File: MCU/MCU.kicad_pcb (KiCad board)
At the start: 4 copper layers, 55 x 62 mm, 52 parts, among them IC1 STM32G474RET6, IC2 ESDA6V1L, J1 Conn_02x04_Top_Bottom, J2 ST-Link, J3 Encoder1, J4 Encoder2, J5 Conn_02x13_Odd_Even, J7 IMU, SW1 SW_Push, SW2 SW_Push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

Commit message: kncoadsnofijasndvoi
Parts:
- R30, R31, R34, R35: footprint Resistor_SMD:R_0603_1608Metric -> Resistor_SMD:R_0805_2012Metric
- moved R31 0.34 mm to (144.6, 75.5)
- moved R35 0.30 mm to (151.8, 75.5)
- moved D5 0.19 mm to (151.5, 77.5)
- moved D4 0.13 mm to (144.2, 77.5)

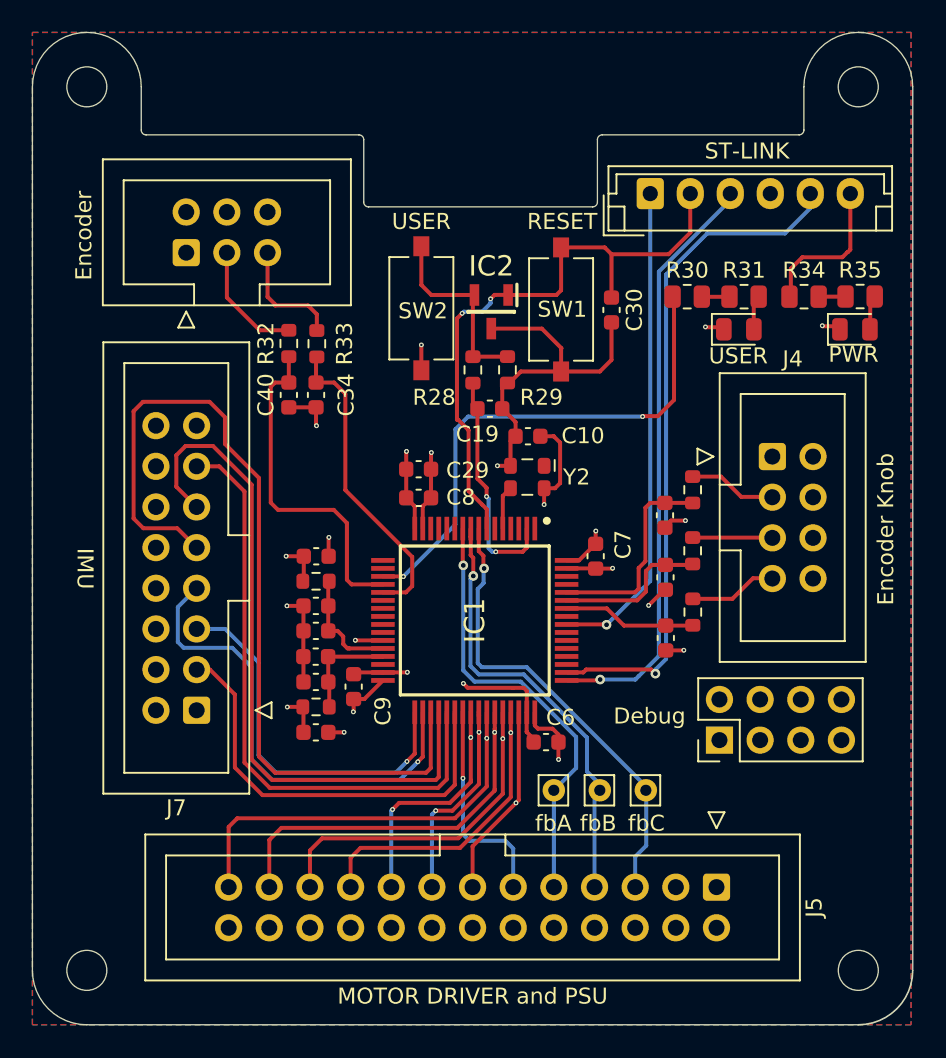
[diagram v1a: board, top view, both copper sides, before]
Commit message: fix all via to 0.45/0.3 mm
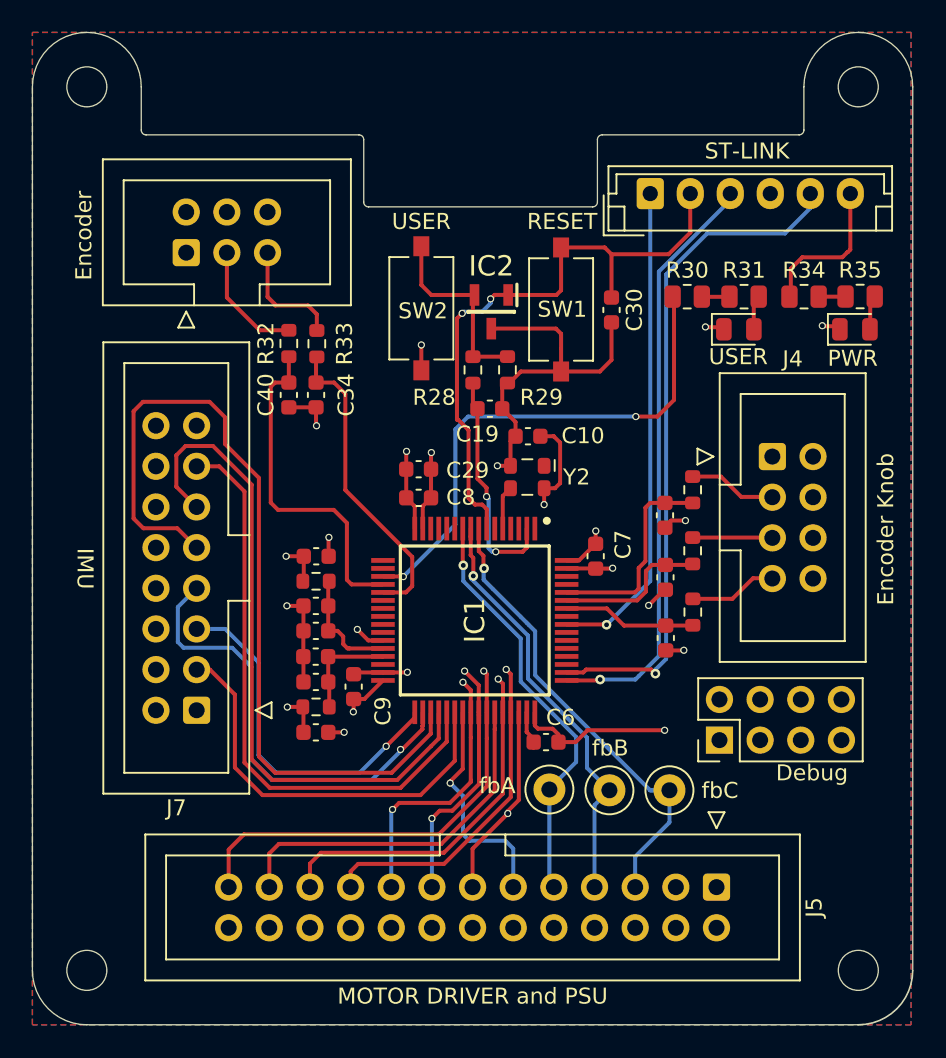
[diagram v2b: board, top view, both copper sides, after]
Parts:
- TP1, TP2, TP3: footprint Connector_Pin:Pin_D0.7mm_L6.5mm_W1.8mm_FlatFork -> TestPoint:TestPoint_Loop_D1.80mm_Drill1.0mm_Beaded
- moved TP1 1.47 mm to (139.9, 106.3)
- moved TP2 0.60 mm to (136.2, 106.3)
- moved TP3 0.28 mm to (132.4, 106.3)
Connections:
- J1 pad 1: /Connector and Sensor/TIM1_CH2 -> /Connector and Sensor/TIM1_CH3
- J1 pad 2: /Connector and Sensor/TIM1_CH2N -> /Connector and Sensor/TIM1_CH2
- J1 pad 3: /Connector and Sensor/TIM1_CH1 -> /Connector and Sensor/TIM1_CH3N
- J1 pad 4: /Connector and Sensor/TIM1_CH1N -> /Connector and Sensor/TIM1_CH2N
- J1 pad 5: /Connector and Sensor/TIM1_CH3 -> /Connector and Sensor/TIM1_CH1
- J1 pad 6: /Connector and Sensor/TIM1_CH3N -> unconnected-(J1-Pin_6-Pad6)
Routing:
- net +5V: track 88.8 -> 118.7 mm
- net /Connector and Sensor/TIM1_CH1N: track 41.8 -> 22.8 mm, vias 1 -> 0
- net /Connector and Sensor/TIM1_CH1: track 45.1 -> 57.1 mm
- net /Connector and Sensor/TIM1_CH2N: track 32.6 -> 39.7 mm
- net VDD: track 37.7 -> 43.6 mm
- net GND: track 60.2 -> 55.7 mm, vias 15 -> 14
- net /Connector and Sensor/TIM1_CH2: track 34.5 -> 37.9 mm
- net /Connector and Sensor/TIM1_CH3N: track 35.5 -> 37.1 mm
- net /Connector and Sensor/TIM1_CH3: track 37.6 -> 36.0 mm
- net /Connector and Sensor/Vcurrfdbk_C: track 27.6 -> 26.1 mm
- net /Connector and Sensor/IMU_MISO: track 43.2 -> 41.8 mm
- net /Connector and Sensor/IMU_MOSI: track 38.3 -> 36.9 mm
- net /Connector and Sensor/IMU_INT2: track 23.8 -> 22.5 mm
- net /Connector and Sensor/IMU_SCLK: track 54.6 -> 53.3 mm
- net /Connector and Sensor/Vcurrfdbk_A: track 29.0 -> 30.2 mm
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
